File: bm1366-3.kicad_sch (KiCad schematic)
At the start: 89 parts, among them U1 25MHz, U14 BM1366_mode1, U25 ADP171AUJ-R7, U26 ADP171AUJ-R7, U28 TLV3544

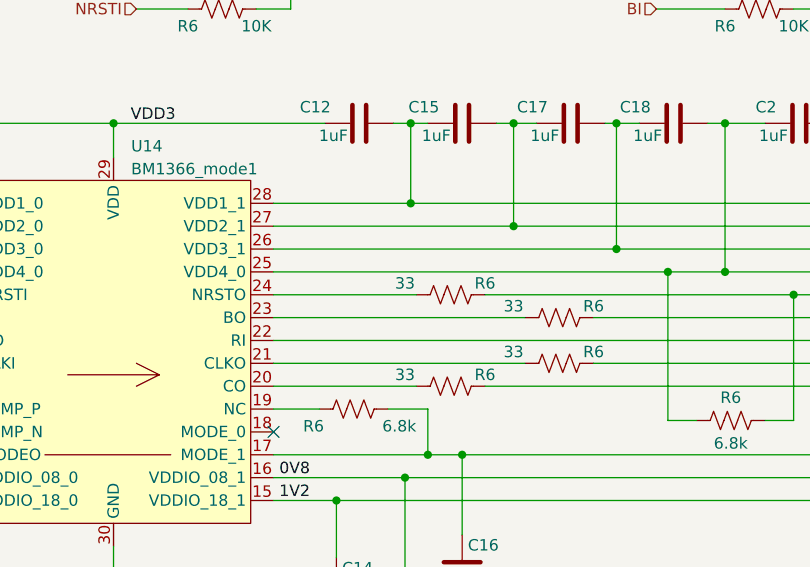
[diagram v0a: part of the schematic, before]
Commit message: Add ESP32 testpoints, fix all DRC errors
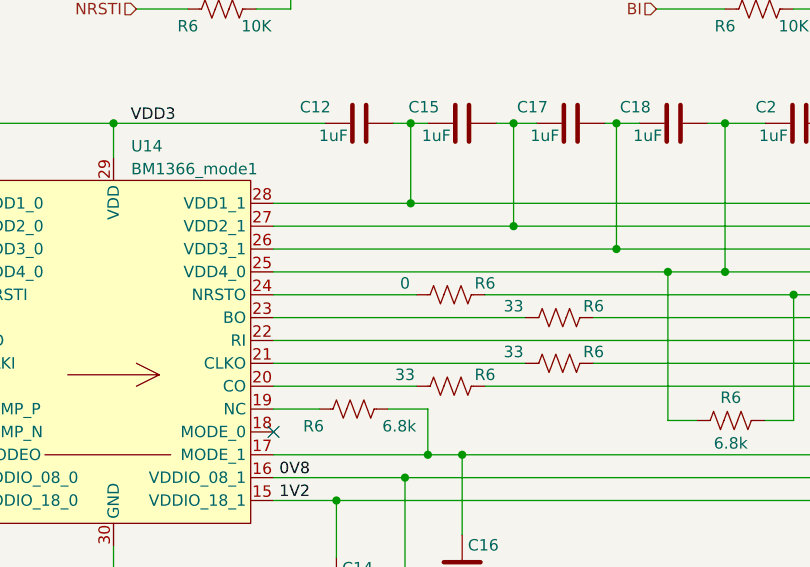
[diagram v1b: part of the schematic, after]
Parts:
- R6: value 33 -> 0
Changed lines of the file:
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@@
       (effects (font (size 1.27 1.27)))
     )
-    (property "Value" "33" (at 106.045 80.645 90)
+    (property "Value" "0" (at 106.045 80.645 90)
       (effects (font (size 1.27 1.27)))
     )

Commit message: BOM mostly completed
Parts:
- R52, R53: DK (none) -> 311-1.00LRCT-ND; PARTNO (none) -> RC0402FR-071RL
- R6: DK (none) -> 311-33.0LRCT-ND; PARTNO (none) -> RC0402FR-0733RL
- R6: value 1K -> 1k; DK (none) -> 311-1.00KLRCT-ND; PARTNO (none) -> RC0402FR-071KL
- R6: value 10K -> 10k; DK (none) -> 311-10KJRCT-ND; PARTNO (none) -> RC0402JR-0710KL
- R6: DK (none) -> 13-RC0402FR-136K8LCT-ND; PARTNO (none) -> RC0402FR-136K8L
- R6: value 130K -> 130k 1%; DK (none) -> YAG2969CT-ND; PARTNO (none) -> RC0402FR-07130KL; Tolerance 1% -> (none)
- R6: value 182K -> 182k 1%; DK (none) -> YAG3015CT-ND; PARTNO (none) -> RC0402FR-07182KL; Tolerance 1% -> (none)
- R6: value 309K -> 309k 1%; DK (none) -> YAG3108CT-ND; PARTNO (none) -> RC0402FR-07309KL; Tolerance 1% -> (none)
- R6: DK (none) -> 311-0.0JRCT-ND; PARTNO (none) -> RC0402JR-070RL
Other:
- title: bitaxeUltraHex -> bitaxeHex

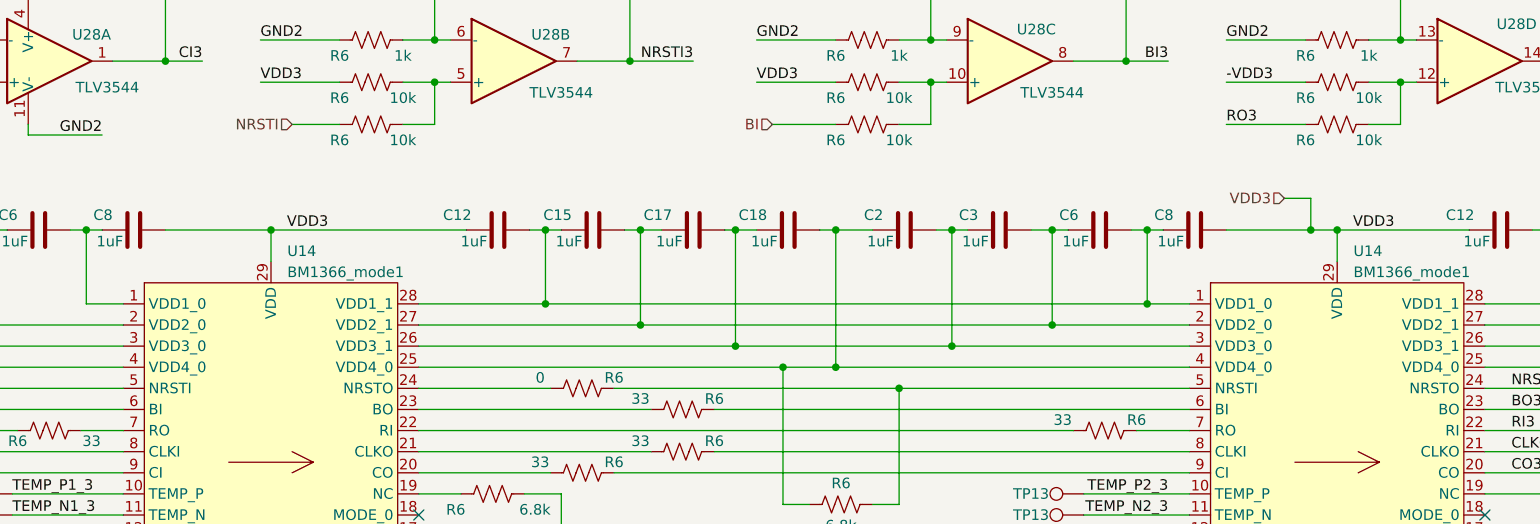
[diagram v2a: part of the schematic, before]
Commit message: link heatsink to schematic and re-link heatsink mounting holes :P
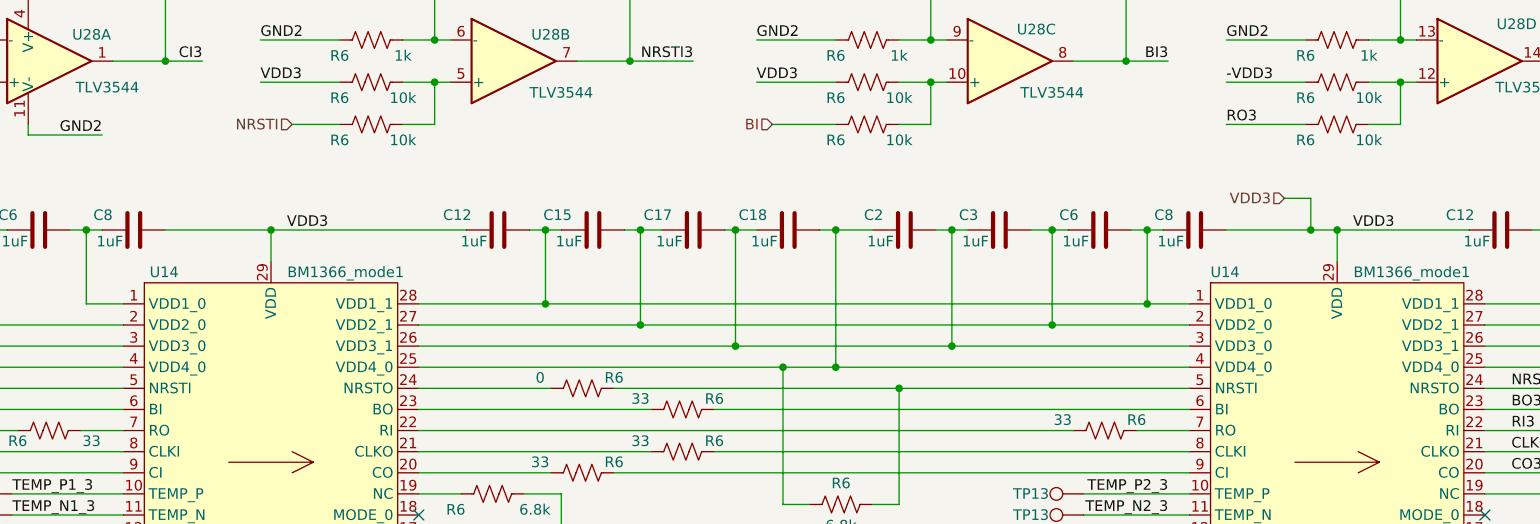
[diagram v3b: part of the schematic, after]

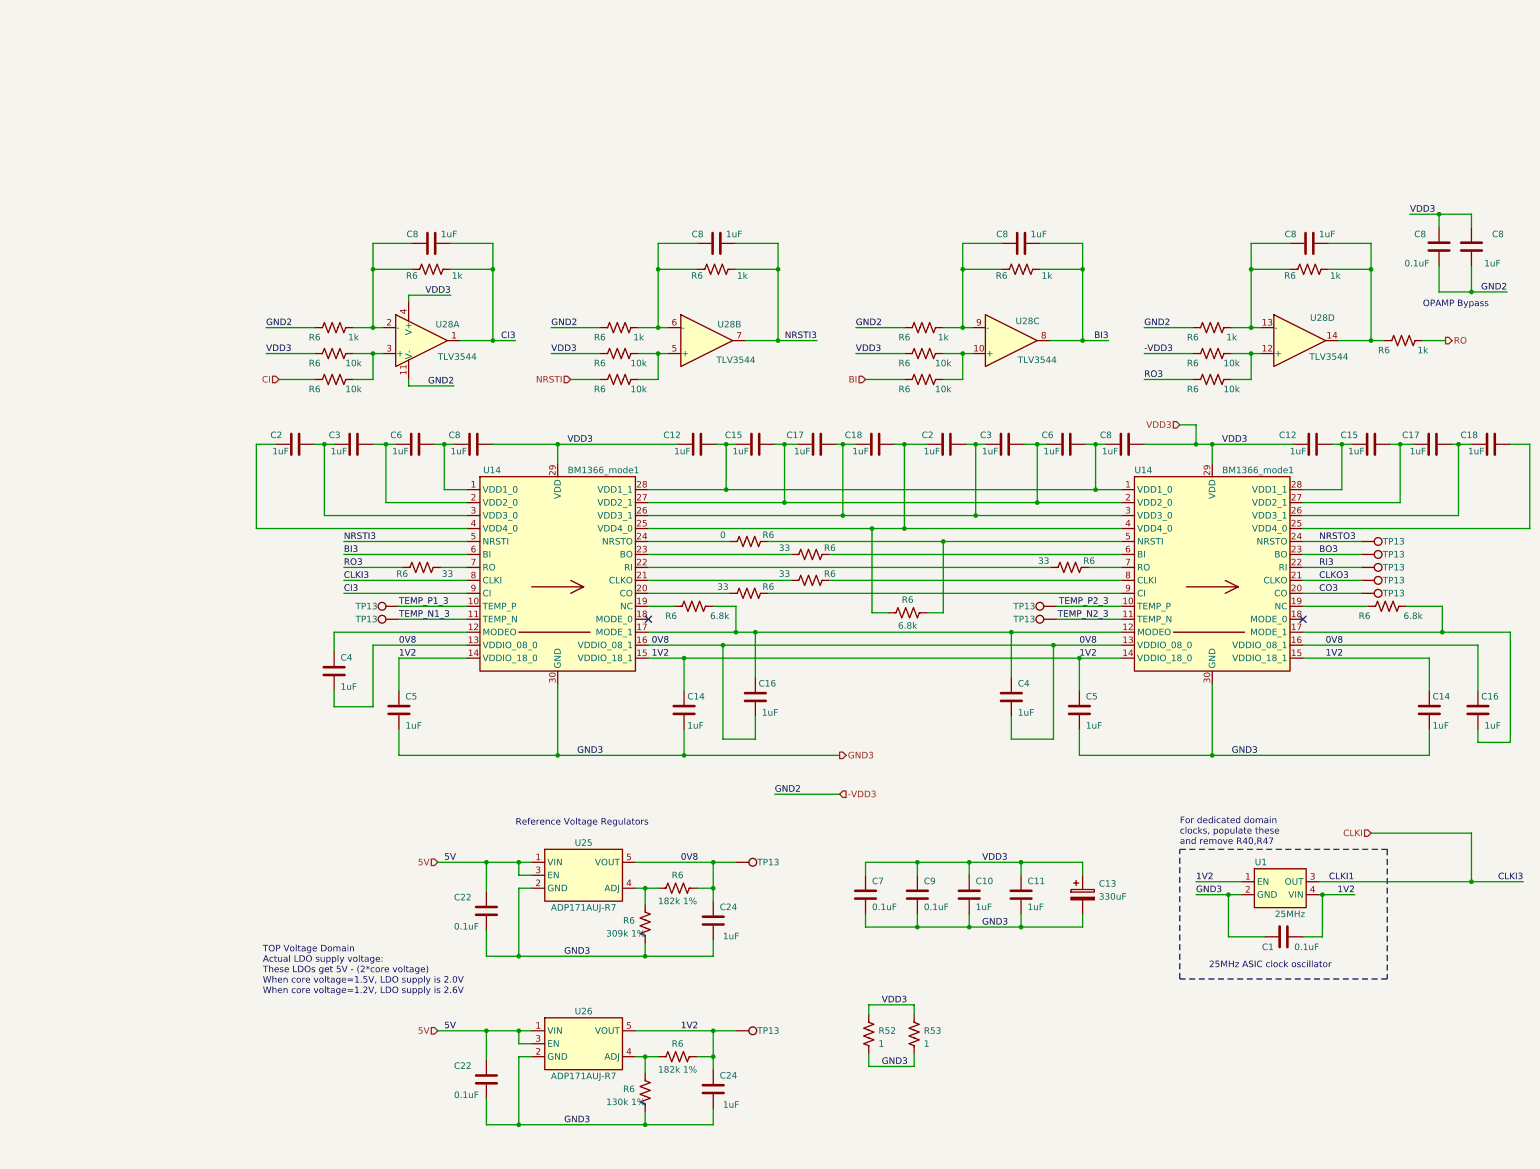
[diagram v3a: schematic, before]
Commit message: sorting out new info on the BM1366 pinouts
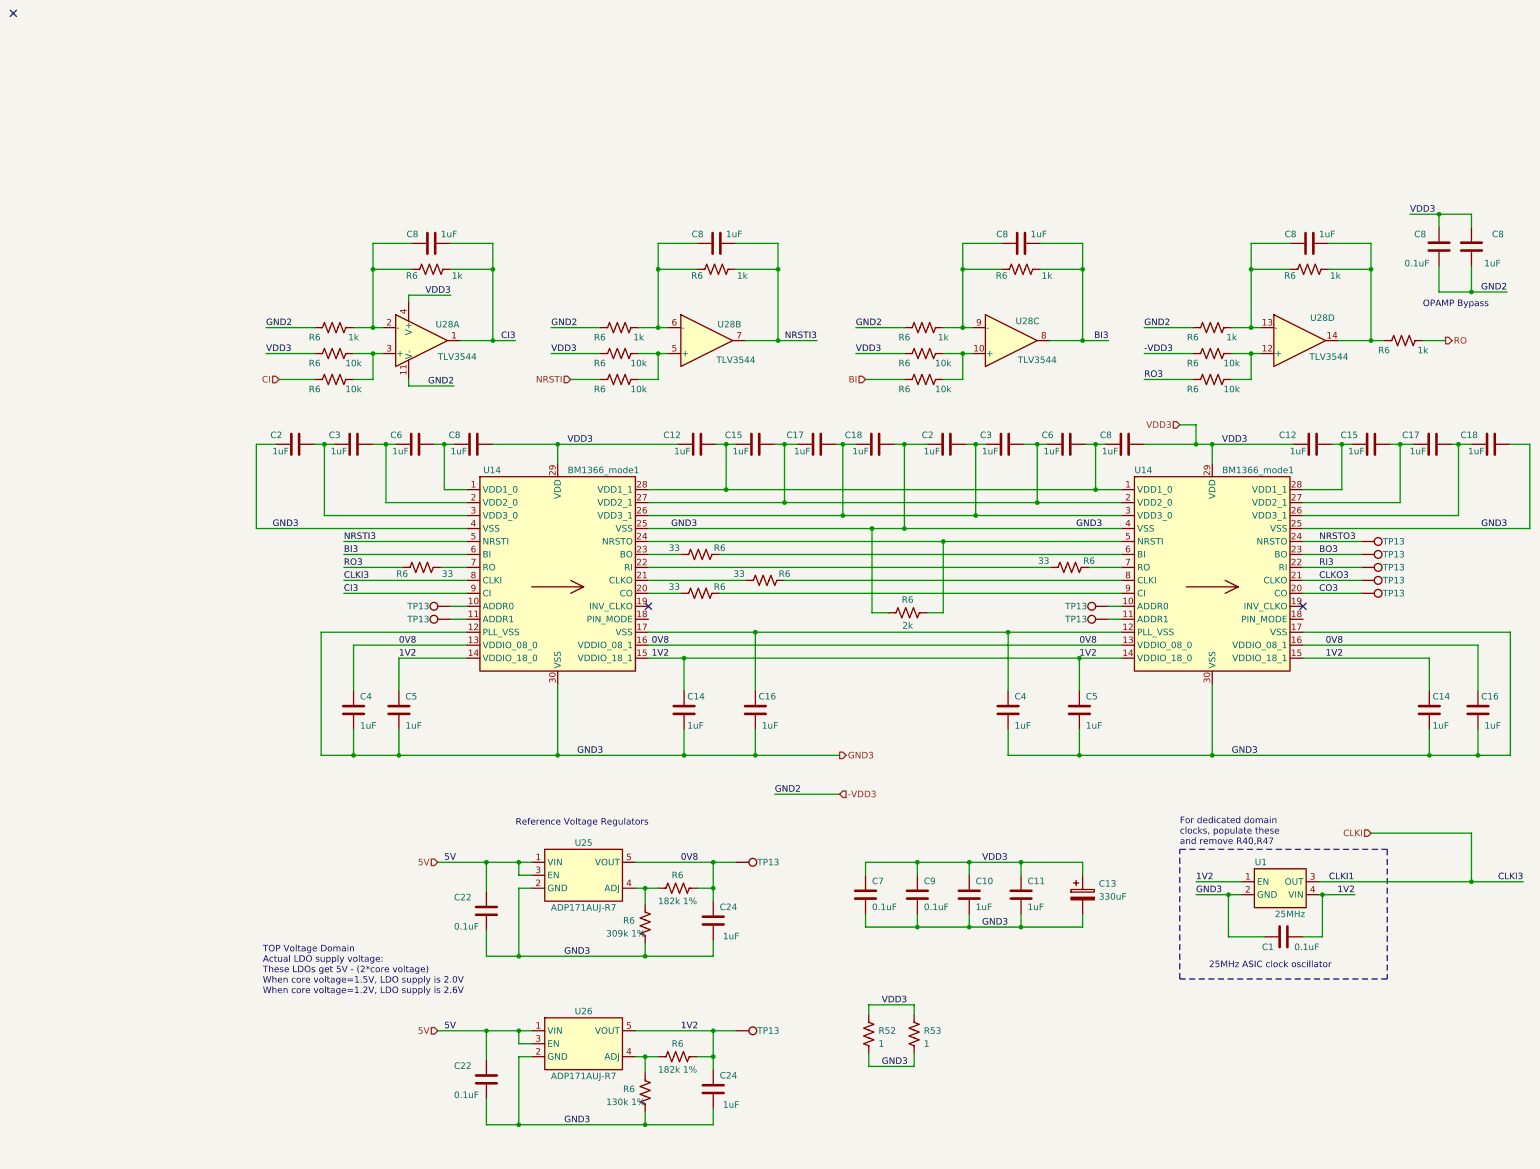
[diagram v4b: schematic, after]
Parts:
- removed R6 (x2): 6.8k, Resistor_SMD:R_0402_1005Metric, symbol Device:R_US
- removed R6: 0, Resistor_SMD:R_0402_1005Metric, symbol Device:R_US
- R6: value 6.8k -> 2k; DK 13-RC0402FR-136K8LCT-ND -> (none); PARTNO RC0402FR-136K8L -> (none)
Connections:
- net 0V8: now also C4.1; no longer C16.2, C4.2, C4.2
- net GND3: now also C16.2, C16.2, C18.2, C18.2, C2.1, C2.1, C4.2, C4.2, R6.1, U14.12 (PLL_VSS), U14.17 (VSS), U14.25 (VSS), U14.25 (VSS), U14.4 (VSS), U14.4 (VSS)
- net at R6.2, U14.5 (NRSTI): now also U14.24 (NRSTO)
- net TEMP_N1_3: no longer names the net of TP13.1, U14.11 (ADDR1)
- net TEMP_N2_3: no longer names the net of TP13.1, U14.11 (ADDR1)
- net TEMP_P1_3: no longer names the net of TP13.1, U14.10 (ADDR0)
- net TEMP_P2_3: no longer names the net of TP13.1, U14.10 (ADDR0)
- no-connect marks 2 -> 3
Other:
- moved on the sheet: C16, C4, R6, TP13
